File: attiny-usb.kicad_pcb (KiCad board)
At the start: 2 copper layers, 41.6 x 16.4 mm, 12 parts, among them J2 Conn_01x06, J3 Conn_01x02, U1 ATtiny85-20P

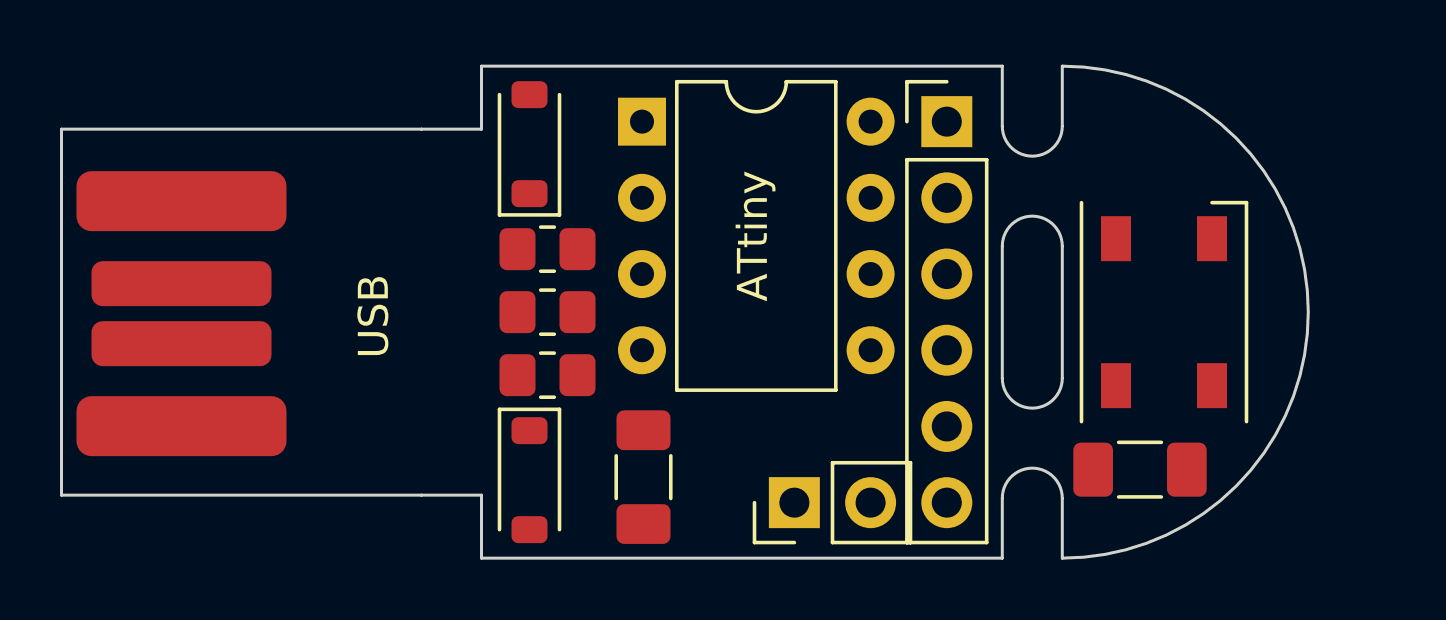
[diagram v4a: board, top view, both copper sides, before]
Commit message: add mouse bite for neopixel
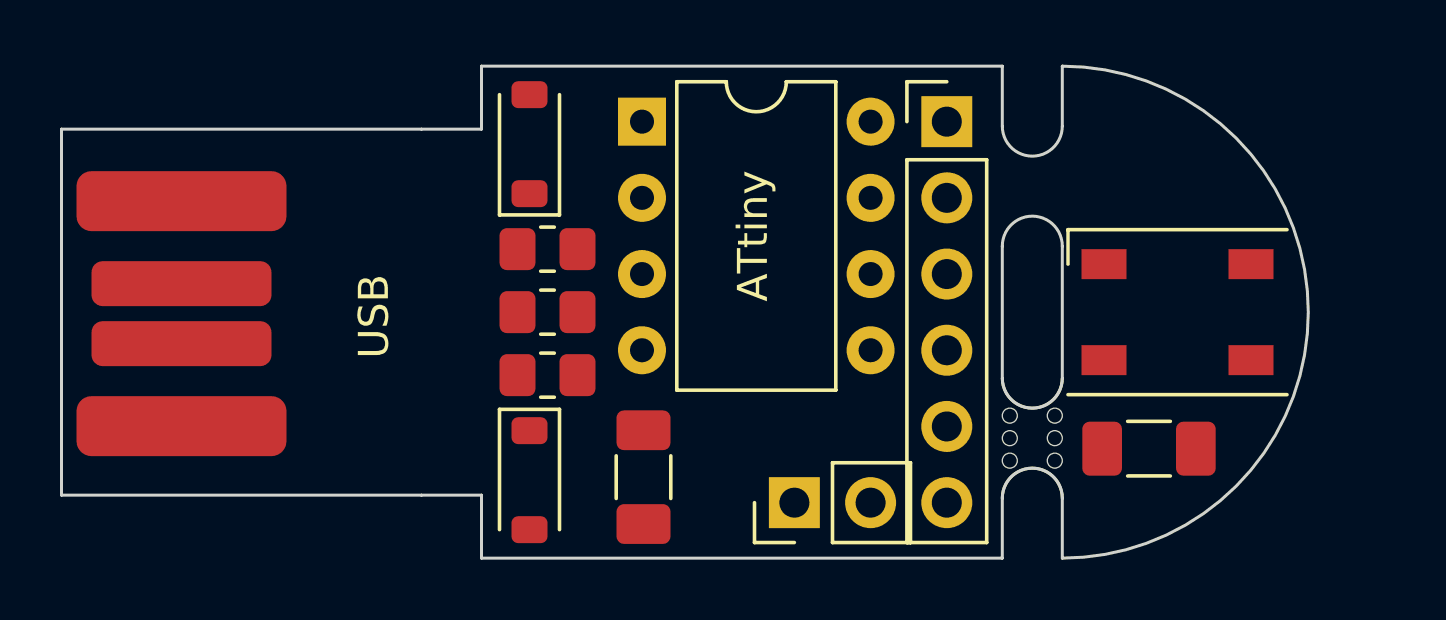
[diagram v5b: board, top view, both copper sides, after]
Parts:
- added mouse-bite-2mm-slot: VAL**, my_lib:mouse-bite-2mm-slot, F.Cu at (132.4, 110.3)
- moved C2 0.76 mm to (136.2, 110.7), turned to 180 degrees
- moved D3 0.45 mm to (137.2, 106.1), turned to 180 degrees
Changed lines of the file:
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@@
   (setup
     (pad_to_mask_clearance 0)
-    (grid_origin 119.35 99.75)
+    (grid_origin 131.36 108.3)
     (pcbplotparams
       (layerselection 0x00010fc_ffffffff)
@@
     )
   )
+  (footprint "my_lib:mouse-bite-2mm-slot" (layer "F.Cu")
+    (at 132.36 110.3 90)
+    (attr through_hole)
+    (fp_text reference "mouse-bite-2mm-slot" (at 0 -2 90) (layer "F.SilkS") hide
+        (effects (font (size 1 1) (thickness 0.2)))
+    )
+    (fp_text value "VAL**" (at 0 2.1 90) (layer "F.SilkS") hide
+        (effects (font (size 1 1) (thickness 0.2)))
+    )
+    (fp_arc (start -2 -1) (mid -1 0) (end -2 1)
+      (stroke (width 0.1) (type solid)) (layer "F.SilkS"))
+    (fp_arc (start 2 1) (mid 1 0) (end 2 -1)
+      (stroke (width 0.1) (type solid)) (layer "F.SilkS"))
+    (fp_circle (center -2 0) (end -2 -0.06)
+      (stroke (width 0.05) (type solid)) (fill none) (layer "Dwgs.User"))
+    (fp_circle (center 2 0) (end 2.06 0)
+      (stroke (width 0.05) (type solid)) (fill none) (layer "Dwgs.User"))
+    (fp_line (start -2 0) (end -2 0)
+      (stroke (width 2) (type solid)) (layer "Eco1.User"))
+    (fp_line (start 2 0) (end 2 0)
+      (stroke (width 2) (type solid)) (layer "Eco1.User"))
+    (pad "" np_thru_hole circle (at -0.75 -0.75 90) (size 0.5 0.5) (drill 0.5) (layers "*.Cu" "*.Mask"))
+    (pad "" np_thru_hole circle (at -0.75 0.75 90) (size 0.5 0.5) (drill 0.5) (layers "*.Cu" "*.Mask"))
+    (pad "" np_thru_hole circle (at 0 -0.75 90) (size 0.5 0.5) (drill 0.5) (layers "*.Cu" "*.Mask"))
+    (pad "" np_thru_hole circle (at 0 0.75 90) (size 0.5 0.5) (drill 0.5) (layers "*.Cu" "*.Mask"))
+    (pad "" np_thru_hole circle (at 0.75 -0.75 90) (size 0.5 0.5) (drill 0.5) (layers "*.Cu" "*.Mask"))
+    (pad "" np_thru_hole circle (at 0.75 0.75 90) (size 0.5 0.5) (drill 0.5) (layers "*.Cu" "*.Mask"))
+  )
   (footprint "my_lib:pcb_usb-connector" (layer "F.Cu")
     (at 104 106.15)
@@
   )
   (footprint "Capacitor_SMD:C_1206_3216Metric_Pad1.33x1.80mm_HandSolder" (layer "F.Cu")
-    (at 135.95 111.35)
+    (at 136.25 110.65 180)
     (descr "Capacitor SMD 1206 (3216 Metric), square (rectangular) end terminal, IPC_7351 nominal with elongated pad for handsoldering. (Body size source: IPC-SM-782 page 76, https://www.pcb-3d.com/wordpress/wp-content/uploads/ipc-sm-782a_amendment_1_and_2.pdf), generated with kicad-footprint-generator")
     (tags "capacitor handsolder")
@@
     (fp_line (start 1.6 0.8) (end -1.6 0.8)
       (stroke (width 0.1) (type solid)) (layer "F.Fab"))
-    (pad "1" smd roundrect (at -1.5625 0) (size 1.325 1.8) (layers "F.Cu" "F.Paste" "F.Mask") (roundrect_rratio 0.188679)
+    (pad "1" smd roundrect (at -1.5625 0 180) (size 1.325 1.8) (layers "F.Cu" "F.Paste" "F.Mask") (roundrect_rratio 0.188679)
       (net 1 "+5V") (pintype "passive"))
-    (pad "2" smd roundrect (at 1.5625 0) (size 1.325 1.8) (layers "F.Cu" "F.Paste" "F.Mask") (roundrect_rratio 0.188679)
+    (pad "2" smd roundrect (at 1.5625 0 180) (size 1.325 1.8) (layers "F.Cu" "F.Paste" "F.Mask") (roundrect_rratio 0.188679)
       (net 2 "GND") (pintype "passive"))
     (model "${KICAD6_3DMODEL_DIR}/Capacitor_SMD.3dshapes/C_1206_3216Metric.wrl"
@@
   )
   (footprint "LED_SMD:LED_SK6812_PLCC4_5.0x5.0mm_P3.2mm" (layer "F.Cu")
-    (at 136.75 106.1 90)
+    (at 137.2 106.1 180)
     (descr "5.0mm x 5.0mm Addressable RGB LED NeoPixel, https://cdn-shop.adafruit.com/product-files/1138/SK6812+LED+datasheet+.pdf")
     (tags "LED RGB NeoPixel PLCC-4 5050")
@@
     (property "ki_keywords" "RGB LED NeoPixel addressable")
     (attr smd)
-    (fp_text reference "D3" (at 0 -3.5 90) (layer "F.SilkS") hide
-        (effects (font (size 1 1) (thickness 0.15)))
-    )
-    (fp_text value "SK6812" (at 0.1 3.55 90) (layer "F.Fab")
-        (effects (font (size 1 1) (thickness 0.15)))
-    )
-    (fp_text user "${REFERENCE}" (at 0 0 90) (layer "F.Fab")
+    (fp_text reference "D3" (at 0 -3.5) (layer "F.SilkS") hide
+        (effects (font (size 1 1) (thickness 0.15)))
+    )
+    (fp_text value "SK6812" (at 0.1 3.55) (layer "F.Fab")
+        (effects (font (size 1 1) (thickness 0.15)))
+    )
+    (fp_text user "${REFERENCE}" (at 0 0) (layer "F.Fab")
         (effects (font (size 0.8 0.8) (thickness 0.15)))
     )
@@
     (fp_circle (center 0 0) (end 0 -2)
       (stroke (width 0.1) (type solid)) (fill none) (layer "F.Fab"))
-    (pad "1" smd rect (at 2.45 1.6 90) (size 1.5 1) (layers "F.Cu" "F.Paste" "F.Mask")
+    (pad "1" smd rect (at 2.45 1.6 180) (size 1.5 1) (layers "F.Cu" "F.Paste" "F.Mask")
       (net 2 "GND") (pinfunction "VSS") (pintype "power_in"))
-    (pad "2" smd rect (at 2.45 -1.6 90) (size 1.5 1) (layers "F.Cu" "F.Paste" "F.Mask")
+    (pad "2" smd rect (at 2.45 -1.6 180) (size 1.5 1) (layers "F.Cu" "F.Paste" "F.Mask")
       (net 5 "Net-(D3-DIN)") (pinfunction "DIN") (pintype "input"))
-    (pad "3" smd rect (at -2.45 -1.6 90) (size 1.5 1) (layers "F.Cu" "F.Paste" "F.Mask")
+    (pad "3" smd rect (at -2.45 -1.6 180) (size 1.5 1) (layers "F.Cu" "F.Paste" "F.Mask")
       (net 1 "+5V") (pinfunction "VDD") (pintype "power_in"))
-    (pad "4" smd rect (at -2.45 1.6 90) (size 1.5 1) (layers "F.Cu" "F.Paste" "F.Mask")
+    (pad "4" smd rect (at -2.45 1.6 180) (size 1.5 1) (layers "F.Cu" "F.Paste" "F.Mask")
       (net 10 "unconnected-(D3-DOUT-Pad4)") (pinfunction "DOUT") (pintype "output"))
     (model "${KICAD7_3DMODEL_DIR}/LED_SMD.3dshapes/LED_SK6812_PLCC4_5.0x5.0mm_P3.2mm.wrl"
@@
   (gr_line (start 112 100) (end 114 100)
     (stroke (width 0.1) (type default)) (layer "Edge.Cuts"))
+  (gr_line (start 112 112.2) (end 114 112.2)
+    (stroke (width 0.1) (type default)) (layer "Edge.Cuts"))
+  (gr_line (start 133.36 108.3) (end 133.36 103.9)
+    (stroke (width 0.1) (type default)) (layer "Edge.Cuts"))
+  (gr_line (start 131.36 103.9) (end 131.36 108.3)
+    (stroke (width 0.1) (type default)) (layer "Edge.Cuts"))
+  (gr_line (start 100 112.2) (end 112 112.2)
+    (stroke (width 0.1) (type default)) (layer "Edge.Cuts"))
+  (gr_arc (start 131.36 112.3) (mid 132.36 111.3) (end 133.36 112.3)
+    (stroke (width 0.1) (type default)) (layer "Edge.Cuts"))
+  (gr_line (start 131.36 114.3) (end 131.36 112.3)
+    (stroke (width 0.1) (type default)) (layer "Edge.Cuts"))
+  (gr_line (start 100 100) (end 112 100)
+    (stroke (width 0.1) (type default)) (layer "Edge.Cuts"))
+  (gr_line (start 133.36 112.3) (end 133.36 114.3)
+    (stroke (width 0.1) (type default)) (layer "Edge.Cuts"))
   (gr_arc (start 133.36 108.3) (mid 132.36 109.3) (end 131.36 108.3)
     (stroke (width 0.1) (type default)) (layer "Edge.Cuts"))
-  (gr_line (start 112 112.2) (end 114 112.2)
-    (stroke (width 0.1) (type default)) (layer "Edge.Cuts"))
-  (gr_line (start 133.36 108.3) (end 133.36 103.9)
-    (stroke (width 0.1) (type default)) (layer "Edge.Cuts"))
-  (gr_line (start 131.36 103.9) (end 131.36 108.3)
-    (stroke (width 0.1) (type default)) (layer "Edge.Cuts"))
-  (gr_arc (start 131.36 112.3) (mid 132.36 111.3) (end 133.36 112.3)
-    (stroke (width 0.1) (type default)) (layer "Edge.Cuts"))
-  (gr_line (start 100 112.2) (end 112 112.2)
-    (stroke (width 0.1) (type default)) (layer "Edge.Cuts"))
-  (gr_line (start 131.36 114.3) (end 131.36 112.3)
-    (stroke (width 0.1) (type default)) (layer "Edge.Cuts"))
-  (gr_line (start 100 100) (end 112 100)
-    (stroke (width 0.1) (type default)) (layer "Edge.Cuts"))
-  (gr_line (start 133.36 112.3) (end 133.36 114.3)
-    (stroke (width 0.1) (type default)) (layer "Edge.Cuts"))
   (gr_arc (start 131.36 103.9) (mid 132.36 102.9) (end 133.36 103.9)
